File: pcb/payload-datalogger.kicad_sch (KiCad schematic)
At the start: 26 parts, among them J1 2.54mm 01x02 header, SW2 PTS815, U1 XIAO-ESP32-C3-DIP, U2 NCP177AMX330TCG, U3 W25X40CLSN

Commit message: Update schematic for DE15
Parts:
- removed D2: B38G3RGB, B38G3RGB:B38G3RGB-10D0003H2U1930_HVK, symbol Device:LED_GBAR
- removed R13: 261, Resistor_SMD:R_0603_1608Metric, symbol Device:R_Small_US
- removed R14, R15: 62, Resistor_SMD:R_0603_1608Metric, symbol Device:R_Small_US
- added D1: B1911USD, LED_SMD:LED_0603_1608Metric, symbol Device:LED
- added J6: DE15, symbol Connector_Generic_Shielded:Conn_01x15_Shielded
- added R13, R14: 10k, symbol Device:R_US
- added R16: 270, Resistor_SMD:R_0603_1608Metric, symbol Device:R_Small_US
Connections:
- net +3V3: now also D1.2 (A), J6.11 (Pin_11), J6.13 (Pin_13)
- net GND: now also J6.SH (Shield), R13.2, R14.2
- net LED_B renamed NTC1-
- net NTC1-: now also J6.14 (Pin_14), R14.1
- net LED_G renamed NTC0-
- net NTC0-: now also J6.12 (Pin_12), R13.1
- net LED_R: no longer names the net of U1.1 (GPIO2/A0/D0)
- net LED_R: now also R16.2
- new net: D1.1 (K), R16.1
- new net TC0+: J6.1 (Pin_1)
- new net TC0-: J6.2 (Pin_2)
- new net TC1+: J6.3 (Pin_3)
- new net TC1-: J6.4 (Pin_4)
- new net TC2+: J6.6 (Pin_6)
- new net TC2-: J6.7 (Pin_7)
- new net TC3+: J6.8 (Pin_8)
- new net TC3-: J6.9 (Pin_9)
- no-connect marks 1 -> 4
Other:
- sheet Thermocouple0 ports: added TC+, TC-; removed none
- sheet Thermocouple1 ports: added TC+, TC-; removed none
- sheet Thermocouple2 ports: added TC+, TC-; removed none
- sheet Thermocouple3 ports: added TC+, TC-; removed none
- note added: "10k NTC thermistor"
- note added: "User LED"
- note removed: "RGB LED"
- moved on the sheet: BT1, C1, C2, C3, J1, R3, R4, U2

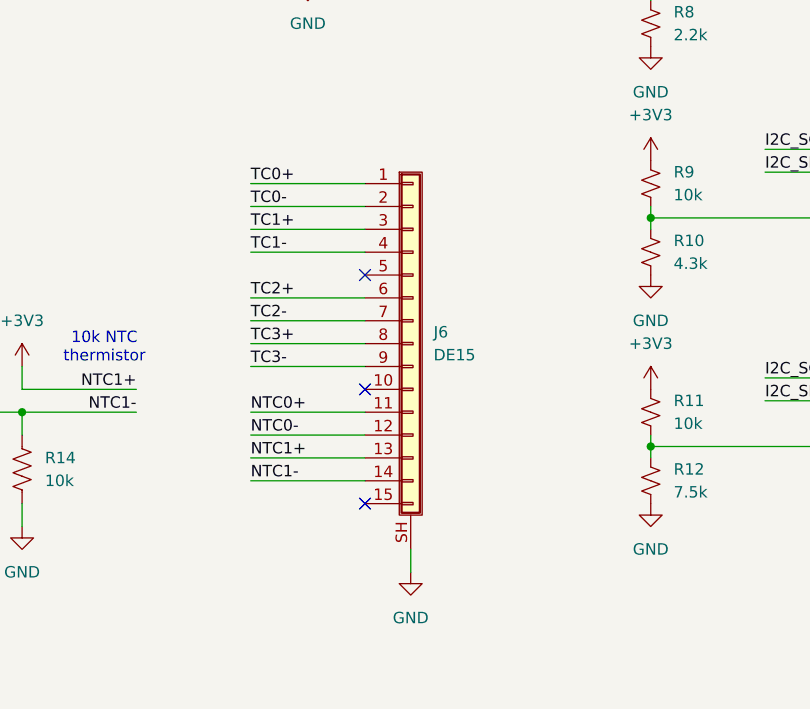
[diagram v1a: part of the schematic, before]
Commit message: Update PCB to use d sub
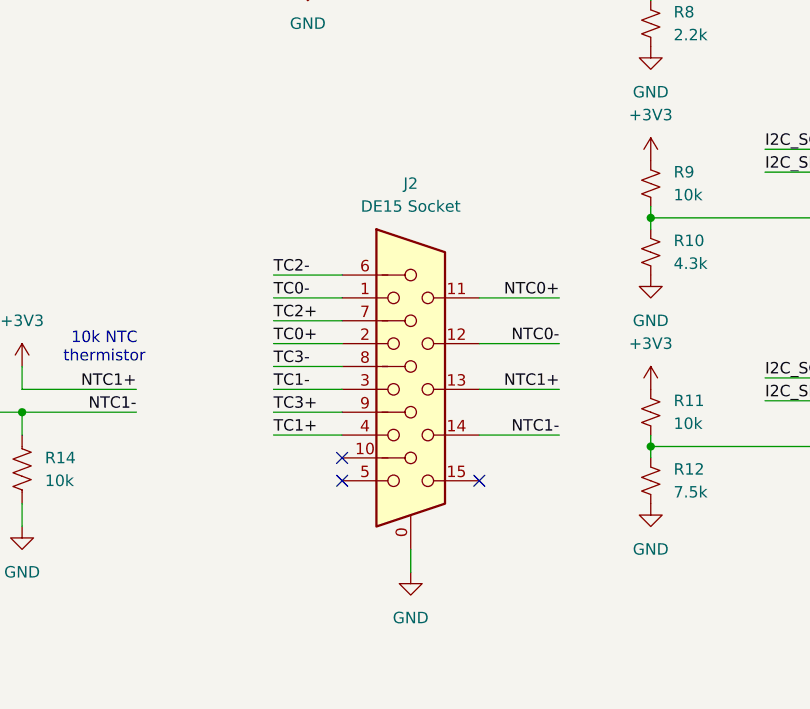
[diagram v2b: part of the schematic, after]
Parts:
- removed J6: DE15, symbol Connector_Generic_Shielded:Conn_01x15_Shielded
- added J2: DE15 Socket, Connector_Dsub:DSUB-15-HD_Socket_Horizontal_P2.29x1.90mm_EdgePinOffset3.03mm_Housed_MountingHolesOffset4.94mm, symbol Connector:DE15_Socket_HighDensity_MountingHoles
- R13, R14: footprint (none) -> Resistor_SMD:R_0603_1608Metric
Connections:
- net +3V3: now also J2.11, J2.13
- net GND: now also J2.0
- net NTC0-: now also J2.12
- net NTC1-: now also J2.14
- net TC0+: now also J2.2
- net TC0-: now also J2.1
- net TC1+: now also J2.4
- net TC1-: now also J2.3
- net TC2+: now also J2.7
- net TC2-: now also J2.6
- net TC3+: now also J2.9
- net TC3-: now also J2.8

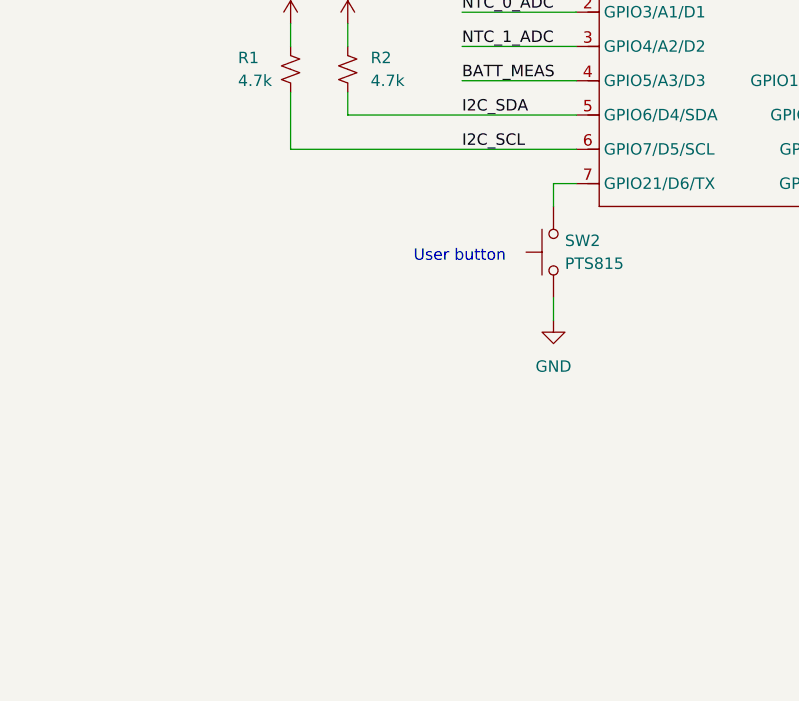
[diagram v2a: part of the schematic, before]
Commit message: Add user button debounce to sch
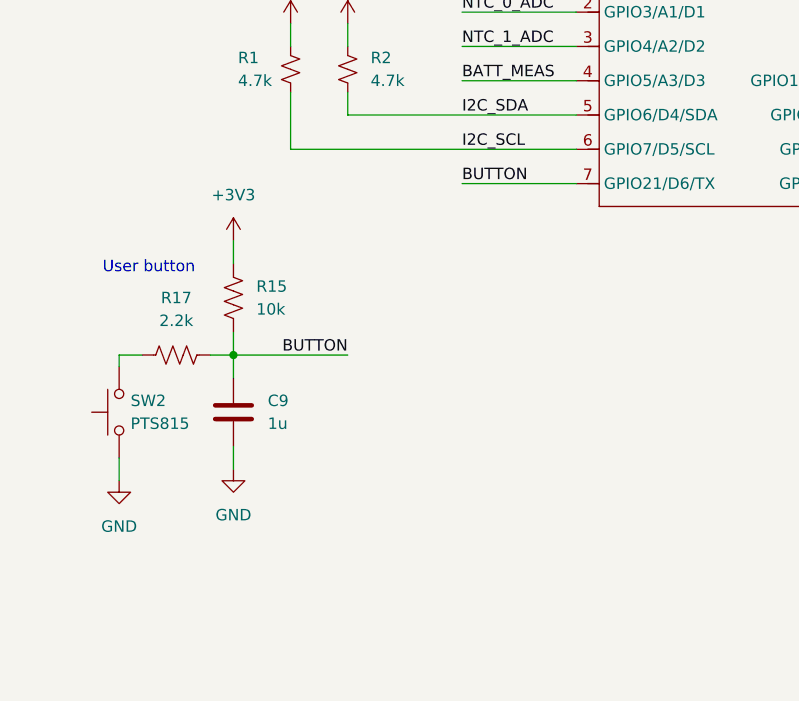
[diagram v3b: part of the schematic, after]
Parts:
- added C9: 1u, symbol Device:C
- added R15: 10k, symbol Device:R_US
- added R17: 2.2k, symbol Device:R_US
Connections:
- net +3V3: now also R15.1
- net GND: now also C9.2
- net at SW2.2: now also R17.1; no longer U1.7 (GPIO21/D6/TX)
- new net BUTTON: C9.1, R15.2, R17.2, U1.7 (GPIO21/D6/TX)
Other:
- moved on the sheet: SW2

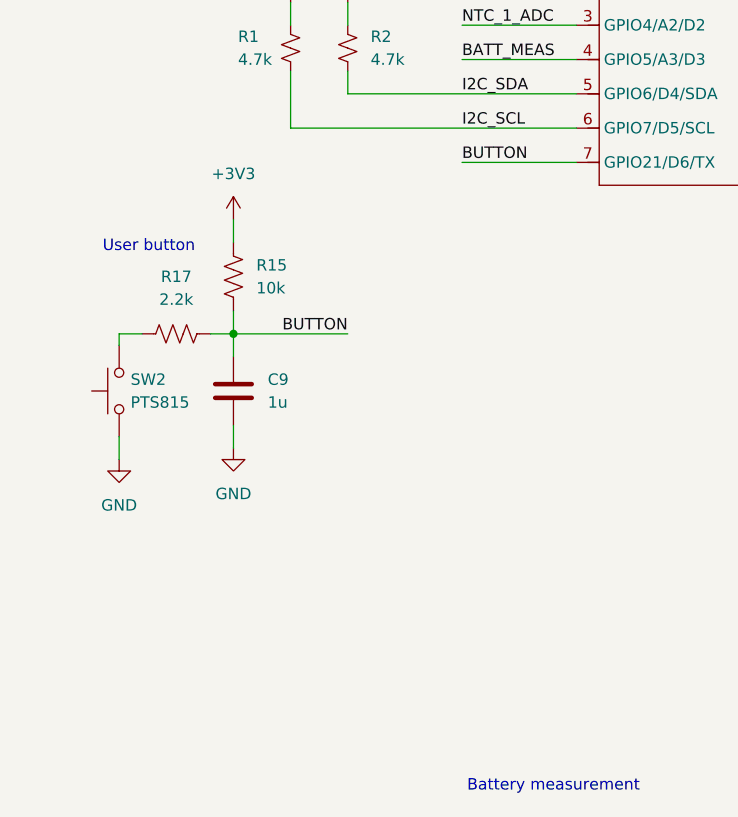
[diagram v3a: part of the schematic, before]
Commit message: Add PCB button debounce
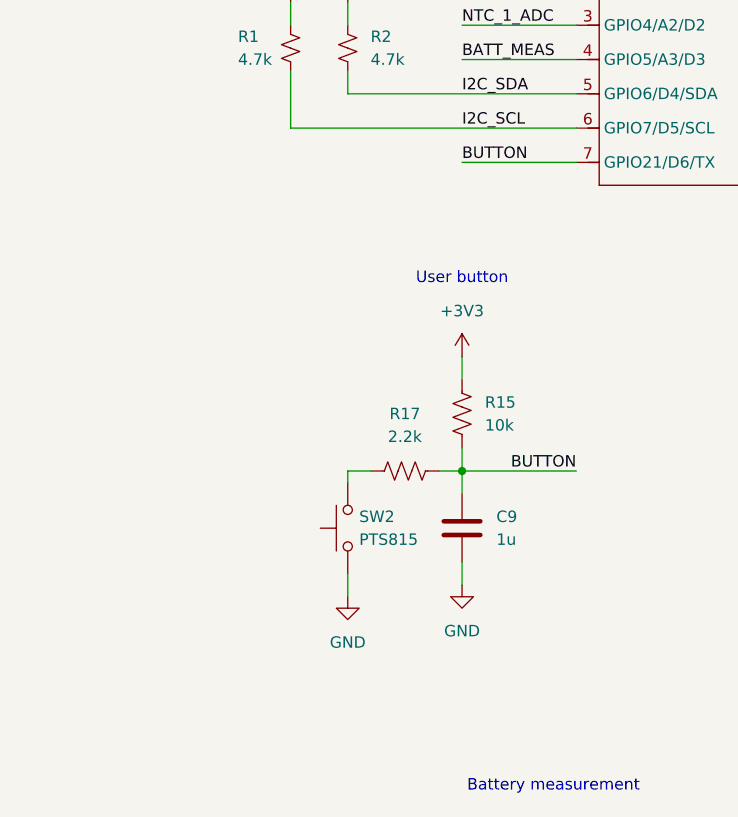
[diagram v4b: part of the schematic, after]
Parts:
- C9: footprint (none) -> Capacitor_SMD:C_0603_1608Metric
- R15, R17: footprint (none) -> Resistor_SMD:R_0603_1608Metric
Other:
- moved on the sheet: C9, R15, R17, SW2
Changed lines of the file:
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@@
 	(text "User button"
 		(exclude_from_sim no)
-		(at 28.702 91.948 0)
+		(at 63.5 95.504 0)
 		(effects
 			(font
@@
 	)
 	(junction
-		(at 38.1 101.6)
+		(at 63.5 116.84)
 		(diameter 0)
 		(color 0 0 0 0)
@@
 	(wire
 		(pts
-			(xy 38.1 101.6) (xy 38.1 104.14)
+			(xy 63.5 116.84) (xy 63.5 119.38)
 		)
 		(stroke
@@
 	(wire
 		(pts
-			(xy 38.1 101.6) (xy 50.8 101.6)
+			(xy 63.5 116.84) (xy 76.2 116.84)
 		)
 		(stroke
@@
 	(wire
 		(pts
-			(xy 38.1 111.76) (xy 38.1 114.3)
+			(xy 63.5 127) (xy 63.5 129.54)
 		)
 		(stroke
@@
 	(wire
 		(pts
-			(xy 25.4 113.03) (xy 25.4 115.57)
+			(xy 50.8 128.27) (xy 50.8 130.81)
 		)
 		(stroke
@@
 	(wire
 		(pts
-			(xy 38.1 101.6) (xy 38.1 99.06)
+			(xy 63.5 116.84) (xy 63.5 114.3)
 		)
 		(stroke
@@
 	(wire
 		(pts
-			(xy 35.56 101.6) (xy 38.1 101.6)
+			(xy 60.96 116.84) (xy 63.5 116.84)
 		)
 		(stroke
@@
 	(wire
 		(pts
-			(xy 38.1 88.9) (xy 38.1 91.44)
+			(xy 63.5 104.14) (xy 63.5 106.68)
 		)
 		(stroke
@@
 	(wire
 		(pts
-			(xy 25.4 101.6) (xy 27.94 101.6)
+			(xy 50.8 116.84) (xy 53.34 116.84)
 		)
 		(stroke
@@
 	(wire
 		(pts
-			(xy 25.4 102.87) (xy 25.4 101.6)
+			(xy 50.8 118.11) (xy 50.8 116.84)
 		)
 		(stroke
@@
 	)
 	(label "BUTTON"
-		(at 50.8 101.6 180)
+		(at 76.2 116.84 180)
 		(effects
 			(font
@@
 	(symbol
 		(lib_id "Switch:SW_Push")
-		(at 25.4 107.95 90)
+		(at 50.8 123.19 90)
 		(unit 1)
 		(exclude_from_sim no)
@@
 		(fields_autoplaced yes)
 		(property "Reference" "SW2"
-			(at 26.67 106.6799 90)
+			(at 52.07 121.9199 90)
 			(effects
 				(font
@@
 		)
 		(property "Value" "PTS815"
-			(at 26.67 109.2199 90)
+			(at 52.07 124.4599 90)
 			(effects
 				(font
@@
 		)
 		(property "Footprint" "PTS815_SJM_250_SMTR_LFS:SW_Push_PTS815_SJM_250_SMTR_LFS"
-			(at 20.32 107.95 0)
+			(at 45.72 123.19 0)
 			(effects
 				(font
@@
 		)
 		(property "Datasheet" "~"
-			(at 20.32 107.95 0)
+			(at 45.72 123.19 0)
 			(effects
 				(font
@@
 		)
 		(property "Description" "Push button switch, generic, two pins"
-			(at 25.4 107.95 0)
+			(at 50.8 123.19 0)
 			(effects
 				(font
@@
 	(symbol
 		(lib_id "Device:C")
-		(at 38.1 107.95 0)
+		(at 63.5 123.19 0)
 		(unit 1)
 		(exclude_from_sim no)
@@
 		(fields_autoplaced yes)
 		(property "Reference" "C9"
-			(at 41.91 106.6799 0)
+			(at 67.31 121.9199 0)
 			(effects
 				(font
@@
 		)
 		(property "Value" "1u"
-			(at 41.91 109.2199 0)
+			(at 67.31 124.4599 0)
 			(effects
 				(font
@@
 			)
 		)
-		(property "Footprint" ""
-			(at 39.0652 111.76 0)
+		(property "Footprint" "Capacitor_SMD:C_0603_1608Metric"
+			(at 64.4652 127 0)
 			(effects
 				(font
@@
 		)
 		(property "Datasheet" "~"
-			(at 38.1 107.95 0)
+			(at 63.5 123.19 0)
 			(effects
 				(font
@@
 		)
 		(property "Description" "Unpolarized capacitor"
-			(at 38.1 107.95 0)
+			(at 63.5 123.19 0)
 			(effects
 				(font
@@
 	(symbol
 		(lib_id "power:GND")
-		(at 38.1 114.3 0)
+		(at 63.5 129.54 0)
 		(unit 1)
 		(exclude_from_sim no)
@@
 		(fields_autoplaced yes)
 		(property "Reference" "#PWR048"
-			(at 38.1 120.65 0)
+			(at 63.5 135.89 0)
 			(effects
 				(font
@@
 		)
 		(property "Value" "GND"
-			(at 38.1 119.38 0)
+			(at 63.5 134.62 0)
 			(effects
 				(font
@@
 		)
 		(property "Footprint" ""
-			(at 38.1 114.3 0)
+			(at 63.5 129.54 0)
 			(effects
 				(font
@@
 		)
 		(property "Datasheet" ""
-			(at 38.1 114.3 0)
+			(at 63.5 129.54 0)
 			(effects
 				(font
@@
 		)
 		(property "Description" "Power symbol creates a global label with name \"GND\" , ground"
-			(at 38.1 114.3 0)
+			(at 63.5 129.54 0)
 			(effects
 				(font
@@
 	(symbol
 		(lib_id "Device:R_US")
-		(at 31.75 101.6 90)
+		(at 57.15 116.84 90)
 		(unit 1)
 		(exclude_from_sim no)
@@
 		(fields_autoplaced yes)
 		(property "Reference" "R17"
-			(at 31.75 95.25 90)
+			(at 57.15 110.49 90)
 			(effects
 				(font
@@
 		)
 		(property "Value" "2.2k"
-			(at 31.75 97.79 90)
+			(at 57.15 113.03 90)
 			(effects
 				(font
@@
 			)
 		)
-		(property "Footprint" ""
-			(at 32.004 100.584 90)
+		(property "Footprint" "Resistor_SMD:R_0603_1608Metric"
+			(at 57.404 115.824 90)
 			(effects
 				(font
@@
 		)
 		(property "Datasheet" "~"
-			(at 31.75 101.6 0)
+			(at 57.15 116.84 0)
 			(effects
 				(font
@@
 		)
 		(property "Description" "Resistor, US symbol"
-			(at 31.75 101.6 0)
+			(at 57.15 116.84 0)
 			(effects
 				(font
@@
 	(symbol
 		(lib_id "Device:R_US")
-		(at 38.1 95.25 0)
+		(at 63.5 110.49 0)
 		(unit 1)
 		(exclude_from_sim no)
@@
 		(fields_autoplaced yes)
 		(property "Reference" "R15"
-			(at 40.64 93.9799 0)
+			(at 66.04 109.2199 0)
 			(effects
 				(font
@@
 		)
 		(property "Value" "10k"
-			(at 40.64 96.5199 0)
+			(at 66.04 111.7599 0)
 			(effects
 				(font
@@
 			)
 		)
-		(property "Footprint" ""
-			(at 39.116 95.504 90)
+		(property "Footprint" "Resistor_SMD:R_0603_1608Metric"
+			(at 64.516 110.744 90)
 			(effects
 				(font
@@
 		)
 		(property "Datasheet" "~"
-			(at 38.1 95.25 0)
+			(at 63.5 110.49 0)
 			(effects
 				(font
@@
 		)
 		(property "Description" "Resistor, US symbol"
-			(at 38.1 95.25 0)
+			(at 63.5 110.49 0)
 			(effects
 				(font
@@
 	(symbol
 		(lib_id "power:GND")
-		(at 25.4 115.57 0)
+		(at 50.8 130.81 0)
 		(unit 1)
 		(exclude_from_sim no)
@@
 		(fields_autoplaced yes)
 		(property "Reference" "#PWR053"
-			(at 25.4 121.92 0)
+			(at 50.8 137.16 0)
 			(effects
 				(font
@@
 		)
 		(property "Value" "GND"
-			(at 25.4 120.65 0)
+			(at 50.8 135.89 0)
 			(effects
 				(font
@@
 		)
 		(property "Footprint" ""
-			(at 25.4 115.57 0)
+			(at 50.8 130.81 0)
 			(effects
 				(font
@@
 		)
 		(property "Datasheet" ""
-			(at 25.4 115.57 0)
+			(at 50.8 130.81 0)
 			(effects
 				(font
@@
 		)
 		(property "Description" "Power symbol creates a global label with name \"GND\" , ground"
-			(at 25.4 115.57 0)
+			(at 50.8 130.81 0)
 			(effects
 				(font
@@
 	(symbol
 		(lib_id "power:+3V3")
-		(at 38.1 88.9 0)
+		(at 63.5 104.14 0)
 		(unit 1)
 		(exclude_from_sim no)
@@
 		(fields_autoplaced yes)
 		(property "Reference" "#PWR052"
-			(at 38.1 92.71 0)
+			(at 63.5 107.95 0)
 			(effects
 				(font
@@
 		)
 		(property "Value" "+3V3"
-			(at 38.1 83.82 0)
+			(at 63.5 99.06 0)
 			(effects
 				(font
@@
 		)
 		(property "Footprint" ""
-			(at 38.1 88.9 0)
+			(at 63.5 104.14 0)
 			(effects
 				(font
@@
 		)
 		(property "Datasheet" ""
-			(at 38.1 88.9 0)
+			(at 63.5 104.14 0)
 			(effects
 				(font
@@
 		)
 		(property "Description" "Power symbol creates a global label with name \"+3V3\""
-			(at 38.1 88.9 0)
+			(at 63.5 104.14 0)
 			(effects
 				(font

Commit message: Use larger Dsub for BOM optimization
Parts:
- J2: footprint Connector_Dsub:DSUB-15-HD_Socket_Horizontal_P2.29x1.90mm_EdgePinOffset3.03mm_Housed_MountingHolesOffset4.94mm -> Connector_Dsub:DSUB-15-HD_Socket_Horizontal_P2.29x2.54mm_EdgePinOffset8.35mm_Housed_MountingHolesOffset10.89mm
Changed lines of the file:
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@@
 			)
 		)
-		(property "Footprint" "Connector_Dsub:DSUB-15-HD_Socket_Horizontal_P2.29x1.90mm_EdgePinOffset3.03mm_Housed_MountingHolesOffset4.94mm"
+		(property "Footprint" "Connector_Dsub:DSUB-15-HD_Socket_Horizontal_P2.29x2.54mm_EdgePinOffset8.35mm_Housed_MountingHolesOffset10.89mm"
 			(at 171.45 101.6 0)
 			(effects
